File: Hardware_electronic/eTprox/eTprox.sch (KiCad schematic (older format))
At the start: 11 parts, among them J1 Conn_01x03, U1 MTCH101

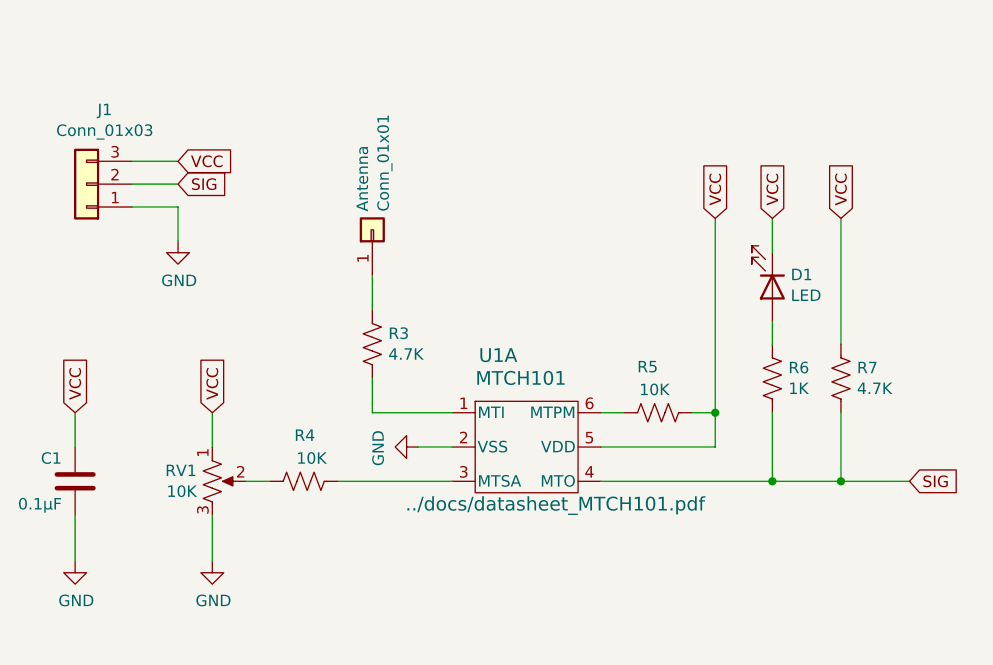
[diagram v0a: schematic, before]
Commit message: Added JST plug
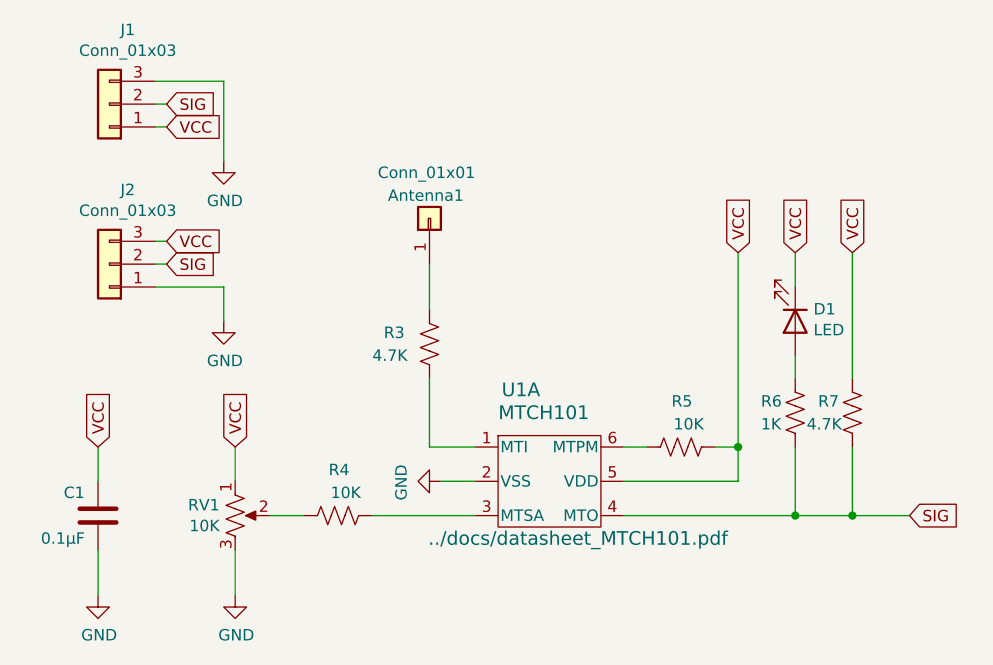
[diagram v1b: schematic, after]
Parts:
- added J2: Conn_01x03, Connector_JST:JST_XH_S3B-XH-A_1x03_P2.50mm_Horizontal, symbol Connector_Generic:Conn_01x03
- renumbered Antenna to Antenna1
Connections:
- net GND: now also J1.3 (Pin_3), J2.1 (Pin_1); no longer J1.1 (Pin_1)
- net SIG: now also J2.2 (Pin_2)
- net VCC: now also J1.1 (Pin_1), J2.3 (Pin_3); no longer J1.3 (Pin_3)
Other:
- moved on the sheet: Antenna1, C1, D1, J1, R3, R4, R5, R6, R7, RV1, U1A

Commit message: Added polarity
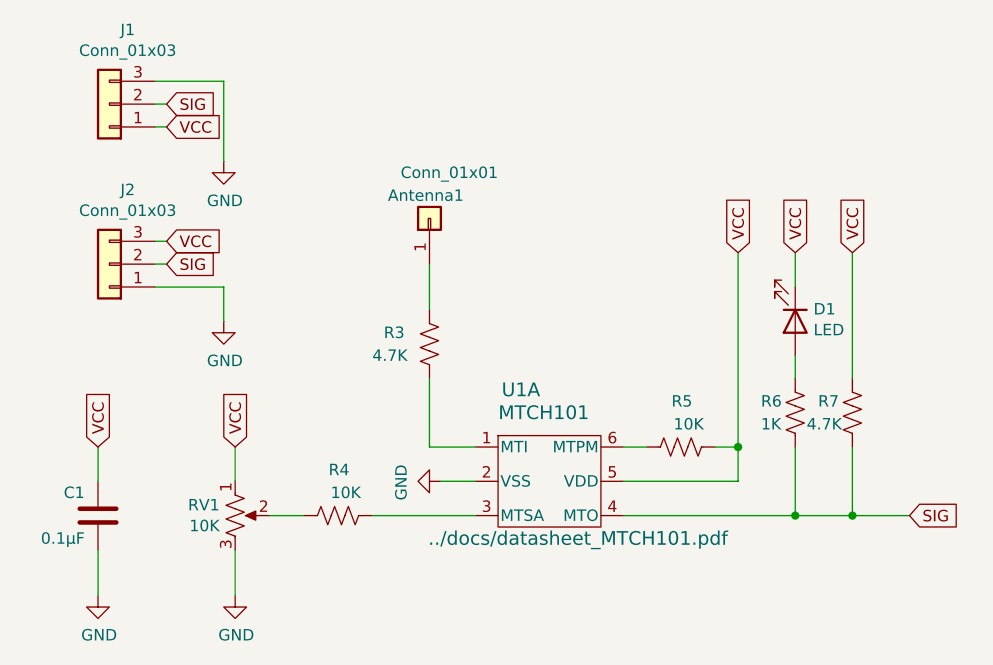
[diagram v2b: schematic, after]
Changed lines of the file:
@@
 P 2700 1800
 F 0 "Antenna1" V 2800 1650 50  0000 L CNN
-F 1 "Conn_01x01" V 2900 1600 50  0000 L CNN
+F 1 "Conn_01x01" V 2900 1500 50  0000 L CNN
 F 2 "eTprox:eTprox_Pad_1x01" H 2700 1800 50  0001 C CNN
 F 3 "~" H 2700 1800 50  0001 C CNN
